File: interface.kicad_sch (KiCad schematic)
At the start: 11 parts

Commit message: だいたい完成
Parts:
- U1, U14: renamed from U?; footprint (none) -> Package_DIP:DIP-14_W7.62mm
- U12, U13, U15, U16: renamed from U?; footprint (none) -> Package_DIP:DIP-20_W7.62mm
- gave numbers to parts that had none: 2
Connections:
- net Data0 is gone; now on net IO_BUS0: U16.2 (A0)
- net Data1 is gone; now on net IO_BUS1: U16.3 (A1)
- net Data2 is gone; now on net IO_BUS2: U16.4 (A2)
- net Data3 is gone; now on net IO_BUS3: U16.5 (A3)
- net Data4 is gone; now on net IO_BUS4: U16.6 (A4)
- net Data5 is gone; now on net IO_BUS5: U16.7 (A5)
- net Data6 is gone; now on net IO_BUS6: U16.8 (A6)
- net Data7 is gone; now on net IO_BUS7: U16.9 (A7)
- net /CE is gone; now on net ~{DE}: U1.13, U12.19 (2OE), U13.19 (2OE), U15.19 (2OE)
- net VCC: now also U12.20 (VCC), U16.20 (VCC)
- net ~{OE}: now also U14.13, U16.1 (A->B)
- net ~{RD}: now also U14.8
- net ~{WE}: now also U14.1
- net ~{WR_CLK}: now also U14.5
- net ~{DE}: now reaches U14.6, U14.9
- net ~{DE}: now also J2.13 (Pin_13), U16.19 (CE)
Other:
- moved on the sheet: J2, J3, U12, U13, U14A, U14B, U14C, U14D, U15, U16, U1F

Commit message: 信号生成部設計完了
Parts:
- renumbered U12 to U13, U13 to U14, U14 to U3
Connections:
- net GND: now also U13.17 (2A0), U13.2 (1A0)
- net ~{WE}: now also U3.12
- net at U3.2, U3.3, U3.4: no longer U3.12
- no-connect marks 52 -> 50
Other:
- moved on the sheet: U3A, U3D

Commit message: 完成版
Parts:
- added D2, D3: LED, LED_THT:LED_D3.0mm, symbol Device:LED
- added R10, R9: R, Resistor_SMD:R_0603_1608Metric_Pad0.98x0.95mm_HandSolder, symbol Device:R
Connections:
- net VCC: now also D2.2 (A), D3.2 (A); no longer J3.37 (Pin_37), J3.39 (Pin_39)
- net ~{OE}: now also R10.2
- net ~{WE}: now also R9.2
- new net: D3.1 (K), R10.1
- new net: D2.1 (K), R9.1
- no-connect marks 50 -> 52
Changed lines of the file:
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@@
   (junction (at 101.6 54.61) (diameter 0) (color 0 0 0 0)
-  )
-  (junction (at 237.49 54.61) (diameter 0) (color 0 0 0 0)
   )
   (junction (at 104.14 95.25) (diameter 0) (color 0 0 0 0)
@@
   (no_connect (at 245.11 74.93))
   (no_connect (at 245.11 69.85))
+  (no_connect (at 245.11 54.61))
+  (no_connect (at 245.11 57.15))
   (no_connect (at 245.11 62.23))
   (no_connect (at 245.11 59.69))
@@
     (stroke (width 0) (type default) (color 0 0 0 0))
   )
-  (wire (pts (xy 237.49 54.61) (xy 237.49 57.15))
-    (stroke (width 0) (type default) (color 0 0 0 0))
-  )
   (wire (pts (xy 232.41 102.87) (xy 245.11 102.87))
     (stroke (width 0) (type default) (color 0 0 0 0))
@@
     (stroke (width 0) (type default) (color 0 0 0 0))
   )
-  (wire (pts (xy 245.11 57.15) (xy 237.49 57.15))
-    (stroke (width 0) (type default) (color 0 0 0 0))
-  )
   (wire (pts (xy 73.66 35.56) (xy 73.66 36.83))
     (stroke (width 0) (type default) (color 0 0 0 0))
@@
     (stroke (width 0) (type default) (color 0 0 0 0))
   )
+  (wire (pts (xy 265.43 133.35) (xy 265.43 134.62))
+    (stroke (width 0) (type default) (color 0 0 0 0))
+  )
   (wire (pts (xy 72.39 151.13) (xy 72.39 163.83))
     (stroke (width 0) (type default) (color 0 0 0 0))
@@
     (stroke (width 0) (type default) (color 0 0 0 0))
   )
+  (wire (pts (xy 243.84 143.51) (xy 243.84 142.24))
+    (stroke (width 0) (type default) (color 0 0 0 0))
+  )
   (wire (pts (xy 113.03 182.88) (xy 133.35 182.88))
     (stroke (width 0) (type default) (color 0 0 0 0))
@@
     (stroke (width 0) (type default) (color 0 0 0 0))
   )
+  (wire (pts (xy 265.43 116.84) (xy 265.43 118.11))
+    (stroke (width 0) (type default) (color 0 0 0 0))
+  )
   (bus (pts (xy 116.84 162.56) (xy 116.84 165.1))
     (stroke (width 0) (type default) (color 0 0 0 0))
@@
     (stroke (width 0) (type default) (color 0 0 0 0))
   )
-  (wire (pts (xy 245.11 54.61) (xy 237.49 54.61))
-    (stroke (width 0) (type default) (color 0 0 0 0))
-  )
   (wire (pts (xy 209.55 124.46) (xy 205.74 124.46))
     (stroke (width 0) (type default) (color 0 0 0 0))
@@
     (stroke (width 0) (type default) (color 0 0 0 0))
   )
-  (wire (pts (xy 237.49 52.07) (xy 237.49 54.61))
-    (stroke (width 0) (type default) (color 0 0 0 0))
-  )
   (wire (pts (xy 158.75 167.64) (xy 168.91 167.64))
     (stroke (width 0) (type default) (color 0 0 0 0))
@@
     (stroke (width 0) (type default) (color 0 0 0 0))
   )
+  (wire (pts (xy 259.08 134.62) (xy 265.43 134.62))
+    (stroke (width 0) (type default) (color 0 0 0 0))
+  )
   (wire (pts (xy 104.14 49.53) (xy 120.65 49.53))
     (stroke (width 0) (type default) (color 0 0 0 0))
@@
     (stroke (width 0) (type default) (color 0 0 0 0))
   )
+  (wire (pts (xy 240.03 143.51) (xy 243.84 143.51))
+    (stroke (width 0) (type default) (color 0 0 0 0))
+  )
   (bus (pts (xy 171.45 165.1) (xy 171.45 162.56))
     (stroke (width 0) (type default) (color 0 0 0 0))
@@
     (stroke (width 0) (type default) (color 0 0 0 0))
   )
+  (wire (pts (xy 243.84 127) (xy 243.84 125.73))
+    (stroke (width 0) (type default) (color 0 0 0 0))
+  )
   (wire (pts (xy 54.61 143.51) (xy 73.66 143.51))
     (stroke (width 0) (type default) (color 0 0 0 0))
@@
     (stroke (width 0) (type default) (color 0 0 0 0))
   )
+  (wire (pts (xy 259.08 118.11) (xy 265.43 118.11))
+    (stroke (width 0) (type default) (color 0 0 0 0))
+  )
   (wire (pts (xy 101.6 146.05) (xy 120.65 146.05))
     (stroke (width 0) (type default) (color 0 0 0 0))
@@
     (stroke (width 0) (type default) (color 0 0 0 0))
   )
+  (wire (pts (xy 243.84 134.62) (xy 251.46 134.62))
+    (stroke (width 0) (type default) (color 0 0 0 0))
+  )
   (wire (pts (xy 102.87 52.07) (xy 120.65 52.07))
     (stroke (width 0) (type default) (color 0 0 0 0))
@@
     (stroke (width 0) (type default) (color 0 0 0 0))
   )
+  (wire (pts (xy 243.84 118.11) (xy 251.46 118.11))
+    (stroke (width 0) (type default) (color 0 0 0 0))
+  )
   (wire (pts (xy 180.34 124.46) (xy 180.34 140.97))
     (stroke (width 0) (type default) (color 0 0 0 0))
@@
   )
   (bus (pts (xy 123.19 135.89) (xy 123.19 97.79))
+    (stroke (width 0) (type default) (color 0 0 0 0))
+  )
+  (wire (pts (xy 240.03 127) (xy 243.84 127))
     (stroke (width 0) (type default) (color 0 0 0 0))
   )
@@
     )
   )
+  (global_label "~{OE}" (shape input) (at 240.03 143.51 180) (fields_autoplaced)
+    (effects (font (size 1.27 1.27)) (justify right))
+    (property "Intersheet References" "${INTERSHEET_REFS}" (id 0) (at 235.1374 143.4306 0)
+      (effects (font (size 1.27 1.27)) (justify right) hide)
+    )
+  )
   (global_label "IO_BUS[0..7]" (shape bidirectional) (at 194.31 78.74 0) (fields_autoplaced)
     (effects (font (size 1.27 1.27)) (justify left))
@@
     )
   )
+  (global_label "~{WE}" (shape input) (at 240.03 127 180) (fields_autoplaced)
+    (effects (font (size 1.27 1.27)) (justify right))
+    (property "Intersheet References" "${INTERSHEET_REFS}" (id 0) (at 235.0164 126.9206 0)
+      (effects (font (size 1.27 1.27)) (justify right) hide)
+    )
+  )
+  (symbol (lib_id "Device:R") (at 243.84 138.43 0) (unit 1)
+    (in_bom yes) (on_board yes) (fields_autoplaced)
+    (property "Reference" "R10" (id 0) (at 246.38 137.1599 0)
+      (effects (font (size 1.27 1.27)) (justify left))
+    )
+    (property "Value" "R" (id 1) (at 246.38 139.6999 0)
+      (effects (font (size 1.27 1.27)) (justify left))
+    )
+    (property "Footprint" "Resistor_SMD:R_0603_1608Metric_Pad0.98x0.95mm_HandSolder" (id 2) (at 242.062 138.43 90)
+      (effects (font (size 1.27 1.27)) hide)
+    )
+    (property "Datasheet" "~" (id 3) (at 243.84 138.43 0)
+      (effects (font (size 1.27 1.27)) hide)
+    )
+    (pin "1")
+    (pin "2")
+  )
   (symbol (lib_id "power:GND") (at 269.24 54.61 0) (mirror y) (unit 1)
     (in_bom yes) (on_board yes)
@@
     )
     (pin "1")
+  )
+  (symbol (lib_id "Device:R") (at 243.84 121.92 0) (unit 1)
+    (in_bom yes) (on_board yes) (fields_autoplaced)
+    (property "Reference" "R9" (id 0) (at 246.38 120.6499 0)
+      (effects (font (size 1.27 1.27)) (justify left))
+    )
+    (property "Value" "R" (id 1) (at 246.38 123.1899 0)
+      (effects (font (size 1.27 1.27)) (justify left))
+    )
+    (property "Footprint" "Resistor_SMD:R_0603_1608Metric_Pad0.98x0.95mm_HandSolder" (id 2) (at 242.062 121.92 90)
+      (effects (font (size 1.27 1.27)) hide)
+    )
+    (property "Datasheet" "~" (id 3) (at 243.84 121.92 0)
+      (effects (font (size 1.27 1.27)) hide)
+    )
+    (pin "1")
+    (pin "2")
   )
   (symbol (lib_id "Connector_Generic:Conn_02x20_Odd_Even") (at 250.19 80.01 0) (mirror x) (unit 1)
@@
     (pin "9")
   )
+  (symbol (lib_id "power:VCC") (at 265.43 133.35 0) (unit 1)
+    (in_bom yes) (on_board yes)
+    (property "Reference" "#PWR070" (id 0) (at 265.43 137.16 0)
+      (effects (font (size 1.27 1.27)) hide)
+    )
+    (property "Value" "VCC" (id 1) (at 261.62 132.08 0))
+    (property "Footprint" "" (id 2) (at 265.43 133.35 0)
+      (effects (font (size 1.27 1.27)) hide)
+    )
+    (property "Datasheet" "" (id 3) (at 265.43 133.35 0)
+      (effects (font (size 1.27 1.27)) hide)
+    )
+    (pin "1")
+  )
   (symbol (lib_id "power:GND") (at 146.05 193.04 0) (unit 1)
     (in_bom yes) (on_board yes)
@@
     (pin "9")
   )
+  (symbol (lib_id "Device:LED") (at 255.27 134.62 0) (unit 1)
+    (in_bom yes) (on_board yes) (fields_autoplaced)
+    (property "Reference" "D3" (id 0) (at 253.6825 128.27 0))
+    (property "Value" "LED" (id 1) (at 253.6825 130.81 0))
+    (property "Footprint" "LED_THT:LED_D3.0mm" (id 2) (at 255.27 134.62 0)
+      (effects (font (size 1.27 1.27)) hide)
+    )
+    (property "Datasheet" "~" (id 3) (at 255.27 134.62 0)
+      (effects (font (size 1.27 1.27)) hide)
+    )
+    (pin "1")
+    (pin "2")
+  )
   (symbol (lib_id "power:VCC") (at 151.13 52.07 0) (mirror y) (unit 1)
     (in_bom yes) (on_board yes)
@@
     )
     (property "Datasheet" "" (id 3) (at 151.13 52.07 0)
+      (effects (font (size 1.27 1.27)) hide)
+    )
+    (pin "1")
+  )
+  (symbol (lib_id "power:VCC") (at 265.43 116.84 0) (unit 1)
+    (in_bom yes) (on_board yes)
+    (property "Reference" "#PWR069" (id 0) (at 265.43 120.65 0)
+      (effects (font (size 1.27 1.27)) hide)
+    )
+    (property "Value" "VCC" (id 1) (at 261.62 115.57 0))
+    (property "Footprint" "" (id 2) (at 265.43 116.84 0)
+      (effects (font (size 1.27 1.27)) hide)
+    )
+    (property "Datasheet" "" (id 3) (at 265.43 116.84 0)
       (effects (font (size 1.27 1.27)) hide)
     )
@@
     (pin "7")
   )
-  (symbol (lib_id "power:VCC") (at 237.49 52.07 0) (mirror y) (unit 1)
-    (in_bom yes) (on_board yes)
-    (property "Reference" "#PWR053" (id 0) (at 237.49 55.88 0)
-      (effects (font (size 1.27 1.27)) hide)
-    )
-    (property "Value" "VCC" (id 1) (at 237.49 48.26 0))
-    (property "Footprint" "" (id 2) (at 237.49 52.07 0)
-      (effects (font (size 1.27 1.27)) hide)
-    )
-    (property "Datasheet" "" (id 3) (at 237.49 52.07 0)
-      (effects (font (size 1.27 1.27)) hide)
-    )
-    (pin "1")
+  (symbol (lib_id "Device:LED") (at 255.27 118.11 0) (unit 1)
+    (in_bom yes) (on_board yes) (fields_autoplaced)
+    (property "Reference" "D2" (id 0) (at 253.6825 111.76 0))
+    (property "Value" "LED" (id 1) (at 253.6825 114.3 0))
+    (property "Footprint" "LED_THT:LED_D3.0mm" (id 2) (at 255.27 118.11 0)
+      (effects (font (size 1.27 1.27)) hide)
+    )
+    (property "Datasheet" "~" (id 3) (at 255.27 118.11 0)
+      (effects (font (size 1.27 1.27)) hide)
+    )
+    (pin "1")
+    (pin "2")
   )
   (symbol (lib_id "power:GND") (at 71.12 35.56 0) (unit 1)

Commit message: 内部バスプルアップ追加他/基板製造バージョン
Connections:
- net VCC: now also J3.37 (Pin_37), J3.39 (Pin_39); no longer J2.37 (Pin_37), J2.39 (Pin_39)
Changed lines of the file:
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@@
   (junction (at 265.43 54.61) (diameter 0) (color 0 0 0 0)
   )
-  (junction (at 151.13 54.61) (diameter 0) (color 0 0 0 0)
-  )
   (junction (at 101.6 146.05) (diameter 0) (color 0 0 0 0)
   )
@@
   )
   (junction (at 180.34 140.97) (diameter 0) (color 0 0 0 0)
+  )
+  (junction (at 237.49 54.61) (diameter 0) (color 0 0 0 0)
   )
   (junction (at 179.07 54.61) (diameter 0) (color 0 0 0 0)
@@
   (no_connect (at 245.11 67.31))
   (no_connect (at 245.11 64.77))
+  (no_connect (at 158.75 54.61))
+  (no_connect (at 158.75 57.15))
   (no_connect (at 257.81 100.33))
   (no_connect (at 257.81 69.85))
@@
   (no_connect (at 245.11 74.93))
   (no_connect (at 245.11 69.85))
-  (no_connect (at 245.11 54.61))
-  (no_connect (at 245.11 57.15))
   (no_connect (at 245.11 62.23))
   (no_connect (at 245.11 59.69))
@@
     (stroke (width 0) (type default) (color 0 0 0 0))
   )
-  (wire (pts (xy 158.75 54.61) (xy 151.13 54.61))
-    (stroke (width 0) (type default) (color 0 0 0 0))
-  )
   (wire (pts (xy 58.42 90.17) (xy 73.66 90.17))
     (stroke (width 0) (type default) (color 0 0 0 0))
@@
     (stroke (width 0) (type default) (color 0 0 0 0))
   )
+  (wire (pts (xy 237.49 52.07) (xy 237.49 54.61))
+    (stroke (width 0) (type default) (color 0 0 0 0))
+  )
   (wire (pts (xy 205.74 121.92) (xy 205.74 119.38))
     (stroke (width 0) (type default) (color 0 0 0 0))
@@
     (stroke (width 0) (type default) (color 0 0 0 0))
   )
-  (wire (pts (xy 151.13 52.07) (xy 151.13 54.61))
-    (stroke (width 0) (type default) (color 0 0 0 0))
-  )
   (wire (pts (xy 119.38 170.18) (xy 133.35 170.18))
     (stroke (width 0) (type default) (color 0 0 0 0))
@@
     (stroke (width 0) (type default) (color 0 0 0 0))
   )
-  (wire (pts (xy 151.13 54.61) (xy 151.13 57.15))
-    (stroke (width 0) (type default) (color 0 0 0 0))
-  )
   (wire (pts (xy 185.42 124.46) (xy 180.34 124.46))
     (stroke (width 0) (type default) (color 0 0 0 0))
@@
     (stroke (width 0) (type default) (color 0 0 0 0))
   )
+  (wire (pts (xy 245.11 57.15) (xy 237.49 57.15))
+    (stroke (width 0) (type default) (color 0 0 0 0))
+  )
   (bus (pts (xy 229.87 74.93) (xy 229.87 77.47))
     (stroke (width 0) (type default) (color 0 0 0 0))
@@
     (stroke (width 0) (type default) (color 0 0 0 0))
   )
+  (wire (pts (xy 237.49 54.61) (xy 237.49 57.15))
+    (stroke (width 0) (type default) (color 0 0 0 0))
+  )
   (wire (pts (xy 104.14 49.53) (xy 104.14 39.37))
     (stroke (width 0) (type default) (color 0 0 0 0))
@@
     (stroke (width 0) (type default) (color 0 0 0 0))
   )
-  (wire (pts (xy 158.75 57.15) (xy 151.13 57.15))
-    (stroke (width 0) (type default) (color 0 0 0 0))
-  )
   (wire (pts (xy 102.87 133.35) (xy 99.06 133.35))
     (stroke (width 0) (type default) (color 0 0 0 0))
@@
   )
   (bus (pts (xy 194.31 78.74) (xy 190.5 78.74))
+    (stroke (width 0) (type default) (color 0 0 0 0))
+  )
+  (wire (pts (xy 245.11 54.61) (xy 237.49 54.61))
     (stroke (width 0) (type default) (color 0 0 0 0))
   )
@@
     (pin "1")
   )
+  (symbol (lib_id "power:VCC") (at 237.49 52.07 0) (mirror y) (unit 1)
+    (in_bom yes) (on_board yes)
+    (property "Reference" "#PWR0101" (id 0) (at 237.49 55.88 0)
+      (effects (font (size 1.27 1.27)) hide)
+    )
+    (property "Value" "VCC" (id 1) (at 237.49 48.26 0))
+    (property "Footprint" "" (id 2) (at 237.49 52.07 0)
+      (effects (font (size 1.27 1.27)) hide)
+    )
+    (property "Datasheet" "" (id 3) (at 237.49 52.07 0)
+      (effects (font (size 1.27 1.27)) hide)
+    )
+    (pin "1")
+  )
   (symbol (lib_id "power:GND") (at 146.05 193.04 0) (unit 1)
     (in_bom yes) (on_board yes)
@@
     (pin "2")
   )
-  (symbol (lib_id "power:VCC") (at 151.13 52.07 0) (mirror y) (unit 1)
-    (in_bom yes) (on_board yes)
-    (property "Reference" "#PWR052" (id 0) (at 151.13 55.88 0)
-      (effects (font (size 1.27 1.27)) hide)
-    )
-    (property "Value" "VCC" (id 1) (at 151.13 48.26 0))
-    (property "Footprint" "" (id 2) (at 151.13 52.07 0)
-      (effects (font (size 1.27 1.27)) hide)
-    )
-    (property "Datasheet" "" (id 3) (at 151.13 52.07 0)
-      (effects (font (size 1.27 1.27)) hide)
-    )
-    (pin "1")
-  )
   (symbol (lib_id "power:VCC") (at 265.43 116.84 0) (unit 1)

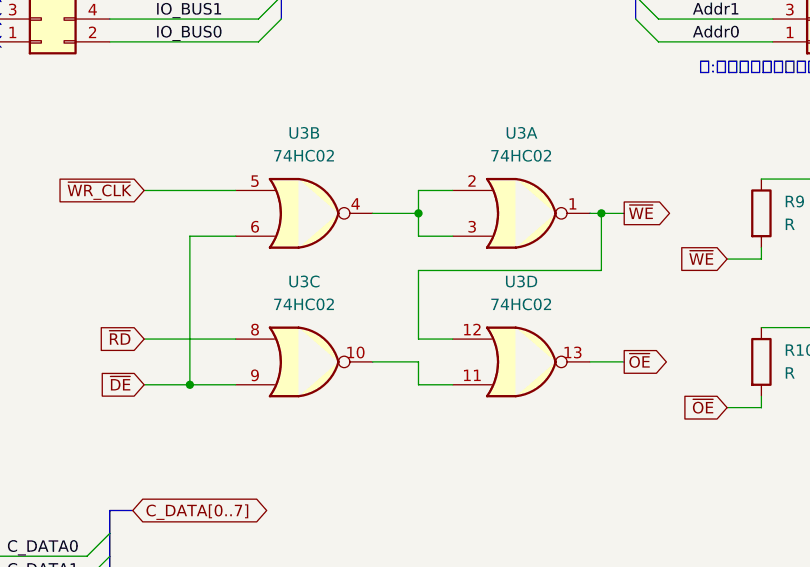
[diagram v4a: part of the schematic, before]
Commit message: VGAの入出力インターフェイス修正
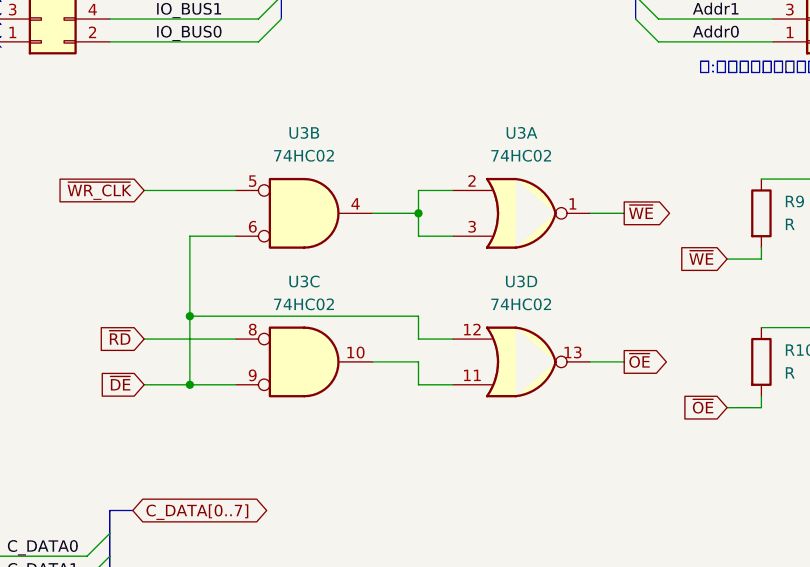
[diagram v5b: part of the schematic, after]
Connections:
- net ~{DE}: now also U3.12
- net ~{WE}: no longer U3.12
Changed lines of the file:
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@@
   (junction (at 101.6 100.33) (diameter 0) (color 0 0 0 0)
   )
-  (junction (at 226.06 121.92) (diameter 0) (color 0 0 0 0)
-  )
   (junction (at 104.14 49.53) (diameter 0) (color 0 0 0 0)
   )
   (junction (at 72.39 105.41) (diameter 0) (color 0 0 0 0)
+  )
+  (junction (at 180.34 133.35) (diameter 0) (color 0 0 0 0)
   )
   (junction (at 72.39 151.13) (diameter 0) (color 0 0 0 0)
@@
     (stroke (width 0) (type default) (color 0 0 0 0))
   )
-  (wire (pts (xy 226.06 128.27) (xy 226.06 121.92))
-    (stroke (width 0) (type default) (color 0 0 0 0))
-  )
   (bus (pts (xy 52.07 52.07) (xy 52.07 54.61))
     (stroke (width 0) (type default) (color 0 0 0 0))
   )
+  (wire (pts (xy 205.74 135.89) (xy 205.74 133.35))
+    (stroke (width 0) (type default) (color 0 0 0 0))
+  )
   (bus (pts (xy 229.87 87.63) (xy 229.87 90.17))
     (stroke (width 0) (type default) (color 0 0 0 0))
@@
     (stroke (width 0) (type default) (color 0 0 0 0))
   )
-  (wire (pts (xy 228.6 121.92) (xy 226.06 121.92))
+  (wire (pts (xy 224.79 121.92) (xy 228.6 121.92))
     (stroke (width 0) (type default) (color 0 0 0 0))
   )
@@
     (stroke (width 0) (type default) (color 0 0 0 0))
   )
-  (wire (pts (xy 226.06 121.92) (xy 224.79 121.92))
-    (stroke (width 0) (type default) (color 0 0 0 0))
-  )
   (bus (pts (xy 173.99 154.94) (xy 171.45 154.94))
     (stroke (width 0) (type default) (color 0 0 0 0))
@@
     (stroke (width 0) (type default) (color 0 0 0 0))
   )
-  (wire (pts (xy 205.74 128.27) (xy 226.06 128.27))
-    (stroke (width 0) (type default) (color 0 0 0 0))
-  )
   (wire (pts (xy 104.14 95.25) (xy 120.65 95.25))
     (stroke (width 0) (type default) (color 0 0 0 0))
@@
     (stroke (width 0) (type default) (color 0 0 0 0))
   )
+  (wire (pts (xy 209.55 135.89) (xy 205.74 135.89))
+    (stroke (width 0) (type default) (color 0 0 0 0))
+  )
   (wire (pts (xy 179.07 62.23) (xy 171.45 62.23))
     (stroke (width 0) (type default) (color 0 0 0 0))
@@
     (stroke (width 0) (type default) (color 0 0 0 0))
   )
-  (wire (pts (xy 205.74 128.27) (xy 205.74 135.89))
-    (stroke (width 0) (type default) (color 0 0 0 0))
-  )
   (wire (pts (xy 105.41 92.71) (xy 120.65 92.71))
     (stroke (width 0) (type default) (color 0 0 0 0))
@@
     (stroke (width 0) (type default) (color 0 0 0 0))
   )
+  (wire (pts (xy 180.34 133.35) (xy 205.74 133.35))
+    (stroke (width 0) (type default) (color 0 0 0 0))
+  )
   (bus (pts (xy 116.84 177.8) (xy 116.84 180.34))
     (stroke (width 0) (type default) (color 0 0 0 0))
@@
     (stroke (width 0) (type default) (color 0 0 0 0))
   )
+  (wire (pts (xy 180.34 133.35) (xy 180.34 140.97))
+    (stroke (width 0) (type default) (color 0 0 0 0))
+  )
   (wire (pts (xy 245.11 54.61) (xy 237.49 54.61))
     (stroke (width 0) (type default) (color 0 0 0 0))
@@
     (stroke (width 0) (type default) (color 0 0 0 0))
   )
-  (wire (pts (xy 180.34 124.46) (xy 180.34 140.97))
+  (wire (pts (xy 180.34 124.46) (xy 180.34 133.35))
     (stroke (width 0) (type default) (color 0 0 0 0))
   )
@@
   )
   (wire (pts (xy 265.43 54.61) (xy 257.81 54.61))
-    (stroke (width 0) (type default) (color 0 0 0 0))
-  )
-  (wire (pts (xy 209.55 135.89) (xy 205.74 135.89))
     (stroke (width 0) (type default) (color 0 0 0 0))
   )
@@
     (pin "1")
   )
-  (symbol (lib_id "74xx:74HC02") (at 193.04 138.43 0) (unit 3)
+  (symbol (lib_id "74xx:74HC02") (at 193.04 138.43 0) (unit 3) (convert 2)
     (in_bom yes) (on_board yes) (fields_autoplaced)
     (property "Reference" "U3" (id 0) (at 193.04 129.54 0))
@@
     (pin "1")
   )
-  (symbol (lib_id "74xx:74HC02") (at 193.04 121.92 0) (unit 2)
+  (symbol (lib_id "74xx:74HC02") (at 193.04 121.92 0) (unit 2) (convert 2)
     (in_bom yes) (on_board yes) (fields_autoplaced)
     (property "Reference" "U3" (id 0) (at 193.04 113.03 0))
